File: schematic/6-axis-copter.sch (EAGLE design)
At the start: 89 parts

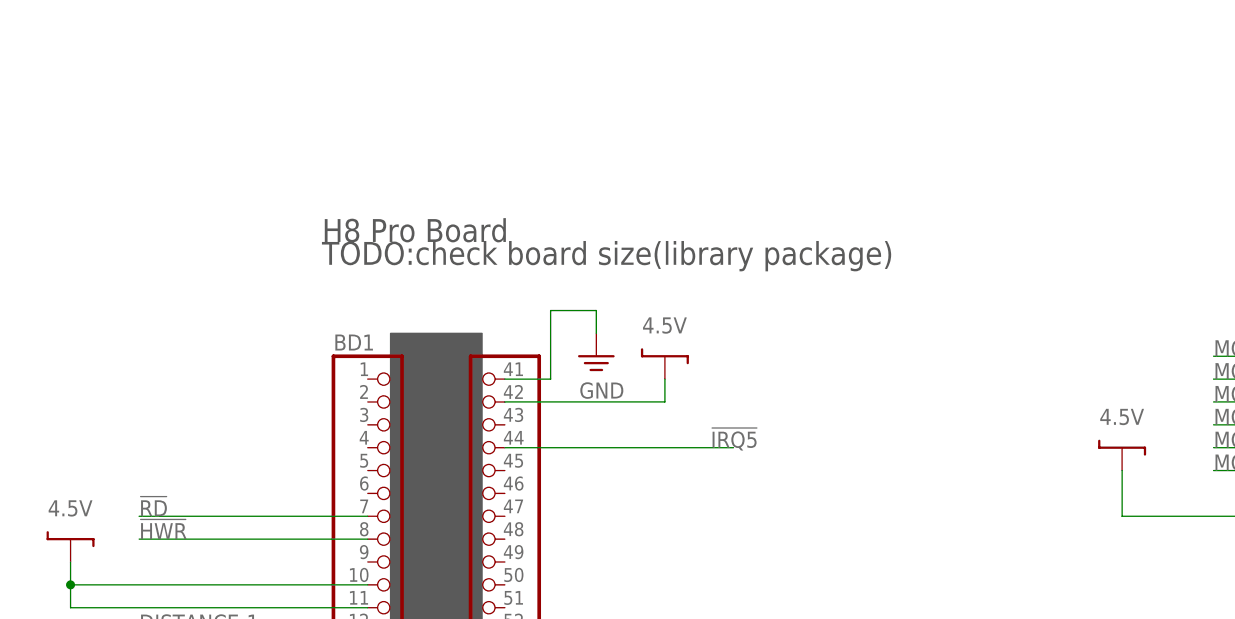
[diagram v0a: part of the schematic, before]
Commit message: IRQ5にプルアップ抵抗追加(オープンドレイン)
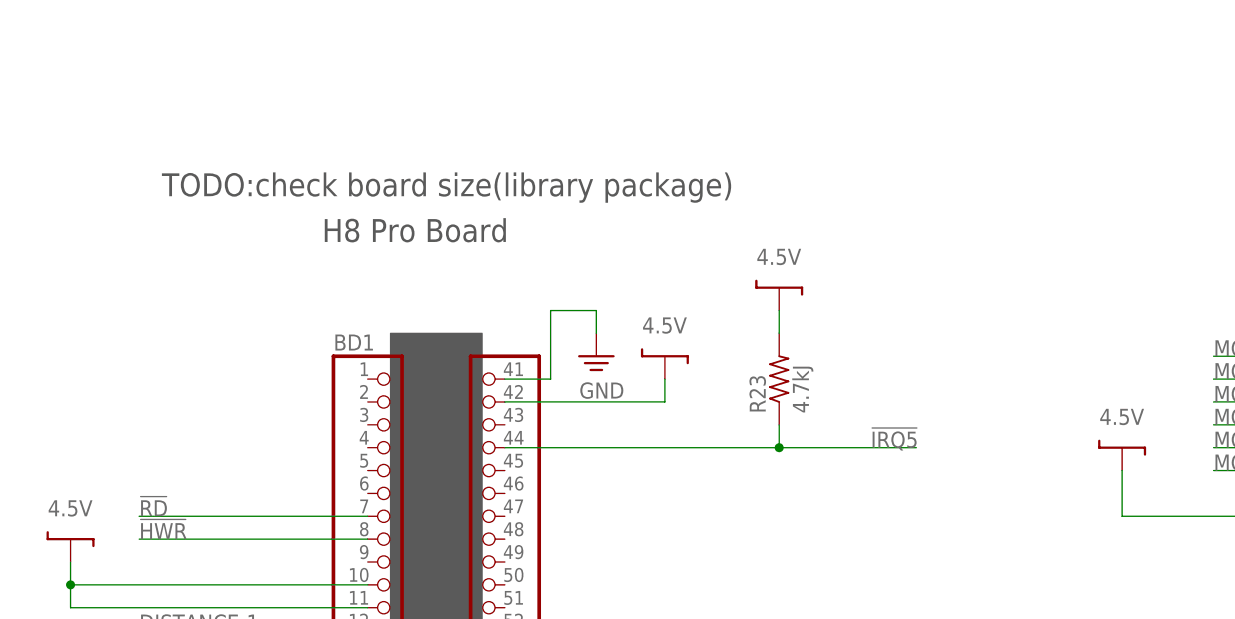
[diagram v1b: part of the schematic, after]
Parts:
- added R23: 4.7kJ, passive:R-US_
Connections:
- net !IRQ5: now also R23.1
- net 4.5V: now also R23.2
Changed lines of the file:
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@@
 <part name="IC19" library="IC" deviceset="PCA9665PW" device=""/>
 <part name="R22" library="passive" deviceset="R-US_" device="" value="1.5kJ"/>
+<part name="P+32" library="symbol" deviceset="4.5V" device=""/>
+<part name="R23" library="passive" deviceset="R-US_" device="" value="4.7kJ"/>
 </parts>
 <sheets>
@@
 </polygon>
 <text x="332.74" y="266.7" size="2.54" layer="97" font="vector">H8 Pro Board</text>
-<text x="332.74" y="264.16" size="2.54" layer="97" font="vector">TODO:check board size(library package)</text>
+<text x="314.96" y="271.78" size="2.54" layer="97" font="vector">TODO:check board size(library package)</text>
 </plain>
 <instances>
@@
 <attribute name="VALUE" x="265.43" y="220.218" size="1.778" layer="96"/>
 </instance>
+<instance part="P+32" gate="G$1" x="383.54" y="261.62"/>
+<instance part="R23" gate="G$1" x="383.54" y="251.46" rot="R90"/>
 </instances>
 <busses>
@@
 <junction x="304.8" y="228.6"/>
 </segment>
+<segment>
+<pinref part="R23" gate="G$1" pin="2"/>
+<pinref part="P+32" gate="G$1" pin="4.5V"/>
+<wire x1="383.54" y1="256.54" x2="383.54" y2="259.08" width="0.1524" layer="91"/>
+</segment>
 </net>
 <net name="N$13" class="0">
@@
 <net name="!IRQ5" class="0">
 <segment>
-<wire x1="378.46" y1="243.84" x2="353.06" y2="243.84" width="0.1524" layer="91"/>
-<label x="375.92" y="243.84" size="1.778" layer="95"/>
+<wire x1="398.78" y1="243.84" x2="383.54" y2="243.84" width="0.1524" layer="91"/>
+<label x="393.7" y="243.84" size="1.778" layer="95"/>
 <pinref part="BD1" gate="G$1" pin="2-4"/>
-</segment>
-<segment>
+<pinref part="R23" gate="G$1" pin="1"/>
+<wire x1="383.54" y1="243.84" x2="353.06" y2="243.84" width="0.1524" layer="91"/>
+<wire x1="383.54" y1="246.38" x2="383.54" y2="243.84" width="0.1524" layer="91"/>
+<junction x="383.54" y="243.84"/>
+</segment>
+<segment>

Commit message: 回路図の不要な配線を削除
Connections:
- removed net !CS2: BD1.1-22
- removed net !UCAS: BD1.1-37
- removed net A10: BD1.2-31
- removed net A2: BD1.2-23
- removed net A3: BD1.2-24
- removed net A4: BD1.2-25
- removed net A5: BD1.2-26
- removed net A6: BD1.2-27
- removed net A7: BD1.2-28
- removed net A8: BD1.2-29
- removed net A9: BD1.2-30
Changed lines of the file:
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@@
-</segment>
-</net>
-<net name="A10" class="0">
-<segment>
-<wire x1="378.46" y1="175.26" x2="353.06" y2="175.26" width="0.1524" layer="91"/>
-<label x="375.92" y="175.26" size="1.778" layer="95"/>
-<pinref part="BD1" gate="G$1" pin="2-31"/>
 </segment>
 </net>
@@
 </segment>
 </net>
-<net name="!CS2" class="0">
-<segment>
-<wire x1="337.82" y1="198.12" x2="312.42" y2="198.12" width="0.1524" layer="91"/>
-<label x="312.42" y="198.12" size="1.778" layer="95"/>
-<pinref part="BD1" gate="G$1" pin="1-22"/>
-</segment>
-</net>
 <net name="!CS1" class="0">
 <segment>
@@
 <wire x1="256.54" y1="226.06" x2="287.02" y2="226.06" width="0.1524" layer="91"/>
 <label x="281.94" y="226.06" size="1.778" layer="95"/>
-</segment>
-</net>
-<net name="!UCAS" class="0">
-<segment>
-<wire x1="337.82" y1="160.02" x2="312.42" y2="160.02" width="0.1524" layer="91"/>
-<label x="312.42" y="160.02" size="1.778" layer="95"/>
-<pinref part="BD1" gate="G$1" pin="1-37"/>
 </segment>
 </net>
@@
 </segment>
 </net>
-<net name="A2" class="0">
-<segment>
-<wire x1="378.46" y1="195.58" x2="353.06" y2="195.58" width="0.1524" layer="91"/>
-<label x="375.92" y="195.58" size="1.778" layer="95"/>
-<pinref part="BD1" gate="G$1" pin="2-23"/>
-</segment>
-</net>
-<net name="A3" class="0">
-<segment>
-<wire x1="378.46" y1="193.04" x2="353.06" y2="193.04" width="0.1524" layer="91"/>
-<label x="375.92" y="193.04" size="1.778" layer="95"/>
-<pinref part="BD1" gate="G$1" pin="2-24"/>
-</segment>
-</net>
-<net name="A4" class="0">
-<segment>
-<wire x1="378.46" y1="190.5" x2="353.06" y2="190.5" width="0.1524" layer="91"/>
-<label x="375.92" y="190.5" size="1.778" layer="95"/>
-<pinref part="BD1" gate="G$1" pin="2-25"/>
-</segment>
-</net>
-<net name="A5" class="0">
-<segment>
-<wire x1="378.46" y1="187.96" x2="353.06" y2="187.96" width="0.1524" layer="91"/>
-<label x="375.92" y="187.96" size="1.778" layer="95"/>
-<pinref part="BD1" gate="G$1" pin="2-26"/>
-</segment>
-</net>
-<net name="A6" class="0">
-<segment>
-<wire x1="378.46" y1="185.42" x2="353.06" y2="185.42" width="0.1524" layer="91"/>
-<label x="375.92" y="185.42" size="1.778" layer="95"/>
-<pinref part="BD1" gate="G$1" pin="2-27"/>
-</segment>
-</net>
-<net name="A7" class="0">
-<segment>
-<wire x1="378.46" y1="182.88" x2="353.06" y2="182.88" width="0.1524" layer="91"/>
-<label x="375.92" y="182.88" size="1.778" layer="95"/>
-<pinref part="BD1" gate="G$1" pin="2-28"/>
-</segment>
-</net>
-<net name="A8" class="0">
-<segment>
-<wire x1="378.46" y1="180.34" x2="353.06" y2="180.34" width="0.1524" layer="91"/>
-<label x="375.92" y="180.34" size="1.778" layer="95"/>
-<pinref part="BD1" gate="G$1" pin="2-29"/>
-</segment>
-</net>
-<net name="A9" class="0">
-<segment>
-<wire x1="378.46" y1="177.8" x2="353.06" y2="177.8" width="0.1524" layer="91"/>
-<label x="375.92" y="177.8" size="1.778" layer="95"/>
-<pinref part="BD1" gate="G$1" pin="2-30"/>
-</segment>
-</net>

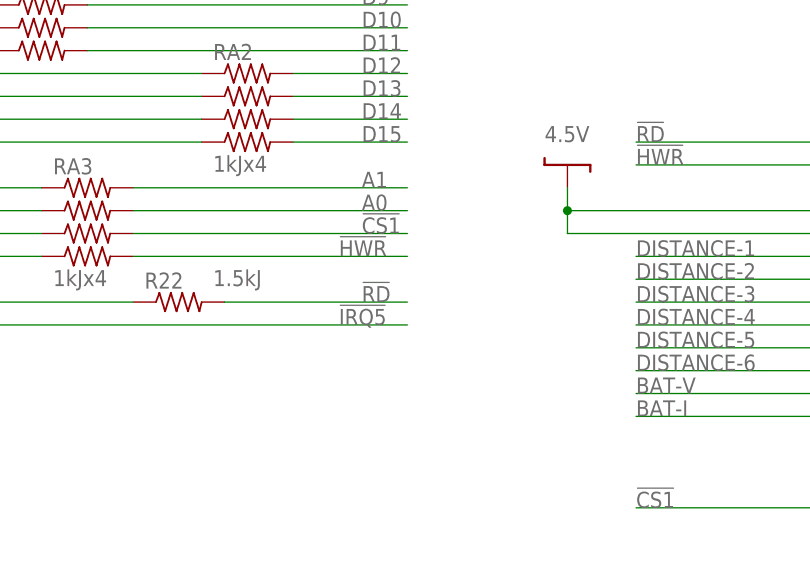
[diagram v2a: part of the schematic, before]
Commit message: 回路図の配線ミスを修正
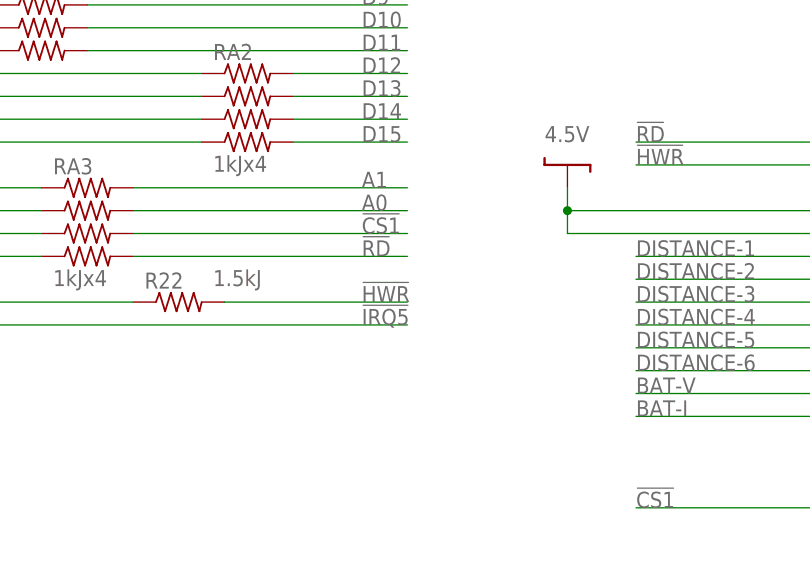
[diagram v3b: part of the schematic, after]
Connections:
- net !HWR: now also R22.2; no longer RA3.5
- net !RD: now also RA3.5; no longer R22.2
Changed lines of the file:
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@@
 </segment>
 <segment>
-<pinref part="R22" gate="G$1" pin="2"/>
-<wire x1="266.7" y1="218.44" x2="287.02" y2="218.44" width="0.1524" layer="91"/>
-<label x="281.94" y="218.44" size="1.778" layer="95"/>
+<pinref part="RA3" gate="G$1" pin="5"/>
+<wire x1="256.54" y1="223.52" x2="287.02" y2="223.52" width="0.1524" layer="91"/>
+<label x="281.94" y="223.52" size="1.778" layer="95"/>
 </segment>
 </net>
@@
 </segment>
 <segment>
-<pinref part="RA3" gate="G$1" pin="5"/>
-<wire x1="256.54" y1="223.52" x2="287.02" y2="223.52" width="0.1524" layer="91"/>
-<label x="279.4" y="223.52" size="1.778" layer="95"/>
+<pinref part="R22" gate="G$1" pin="2"/>
+<wire x1="266.7" y1="218.44" x2="287.02" y2="218.44" width="0.1524" layer="91"/>
+<label x="281.94" y="218.44" size="1.778" layer="95"/>
 </segment>
 </net>
@@
 <pinref part="IC19" gate="G$1" pin="!INT"/>
 <wire x1="233.68" y1="215.9" x2="287.02" y2="215.9" width="0.1524" layer="91"/>
-<label x="279.4" y="215.9" size="1.778" layer="95"/>
+<label x="281.94" y="215.9" size="1.778" layer="95"/>
 </segment>
 </net>

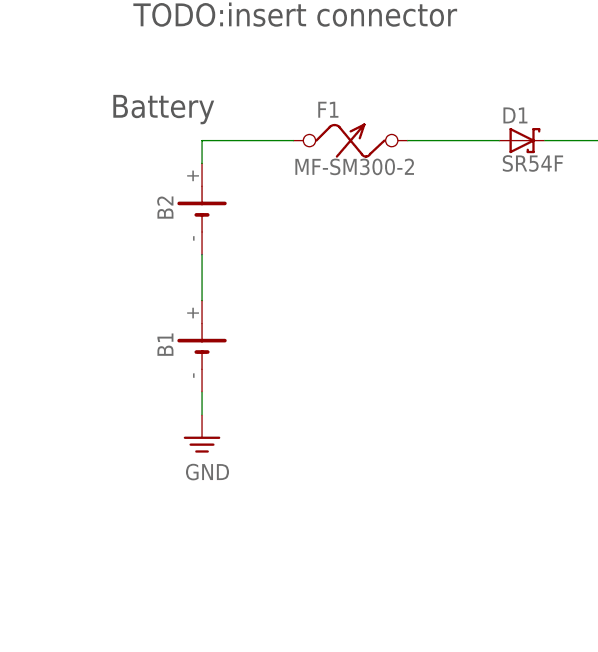
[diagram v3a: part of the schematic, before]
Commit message: 回路図のバッテリーシンボル・フットプリント修正
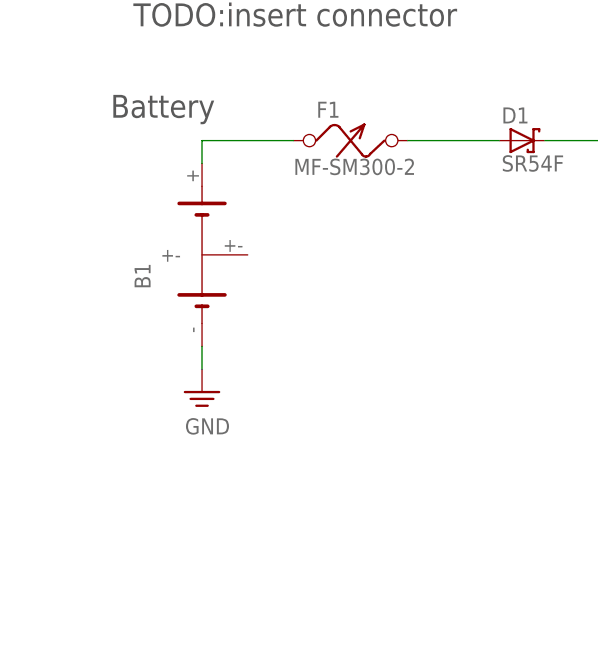
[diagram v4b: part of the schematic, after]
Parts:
- removed B2: (no value), symbol:LIPO-BATT
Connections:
- removed net N$13: B1.+, B2.-
- net N$23: now also B1.+; no longer B2.+
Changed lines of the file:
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@@
 <part name="P+18" library="symbol" deviceset="4.5V" device=""/>
 <part name="P+19" library="symbol" deviceset="4.5V" device=""/>
-<part name="B1" library="symbol" deviceset="LIPO-BATT" device=""/>
-<part name="B2" library="symbol" deviceset="LIPO-BATT" device=""/>
 <part name="SUPPLY14" library="symbol" deviceset="GND" device=""/>
 <part name="P+20" library="symbol" deviceset="BAT" device=""/>
@@
 <part name="P+32" library="symbol" deviceset="4.5V" device=""/>
 <part name="R23" library="passive" deviceset="R-US_" device="" value="4.7kJ"/>
+<part name="B1" library="symbol" deviceset="LIPO-BATT" device=""/>
 </parts>
 <sheets>
@@
 <instance part="P+18" gate="G$1" x="60.96" y="180.34"/>
 <instance part="P+19" gate="G$1" x="60.96" y="154.94"/>
-<instance part="B1" gate="G$1" x="40.64" y="73.66" rot="R90"/>
-<instance part="B2" gate="G$1" x="40.64" y="88.9" rot="R90"/>
-<instance part="SUPPLY14" gate="PE" x="40.64" y="63.5"/>
+<instance part="SUPPLY14" gate="PE" x="40.64" y="68.58"/>
 <instance part="P+20" gate="G$1" x="144.78" y="101.6"/>
 <instance part="IC14" gate="G$1" x="210.82" y="81.28"/>
@@
 <instance part="P+32" gate="G$1" x="383.54" y="261.62"/>
 <instance part="R23" gate="G$1" x="383.54" y="251.46" rot="R90"/>
+<instance part="B1" gate="G$1" x="40.64" y="78.74" rot="R90"/>
 </instances>
 <busses>
@@
 </segment>
 <segment>
+<pinref part="SUPPLY14" gate="PE" pin="GND"/>
+<wire x1="40.64" y1="73.66" x2="40.64" y2="71.12" width="0.1524" layer="91"/>
 <pinref part="B1" gate="G$1" pin="-"/>
-<pinref part="SUPPLY14" gate="PE" pin="GND"/>
-<wire x1="40.64" y1="68.58" x2="40.64" y2="66.04" width="0.1524" layer="91"/>
 </segment>
 <segment>
@@
 <pinref part="P+32" gate="G$1" pin="4.5V"/>
 <wire x1="383.54" y1="256.54" x2="383.54" y2="259.08" width="0.1524" layer="91"/>
-</segment>
-</net>
-<net name="N$13" class="0">
-<segment>
-<pinref part="B2" gate="G$1" pin="-"/>
-<pinref part="B1" gate="G$1" pin="+"/>
-<wire x1="40.64" y1="83.82" x2="40.64" y2="78.74" width="0.1524" layer="91"/>
 </segment>
 </net>
@@
 <pinref part="F1" gate="G$1" pin="1"/>
 <wire x1="50.8" y1="96.52" x2="40.64" y2="96.52" width="0.1524" layer="91"/>
-<pinref part="B2" gate="G$1" pin="+"/>
 <wire x1="40.64" y1="96.52" x2="40.64" y2="93.98" width="0.1524" layer="91"/>
-</segment>
-</net>
+<pinref part="B1" gate="G$1" pin="+"/>
+</segment>
+</net>
